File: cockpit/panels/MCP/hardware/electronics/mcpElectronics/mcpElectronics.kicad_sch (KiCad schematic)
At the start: 12 parts

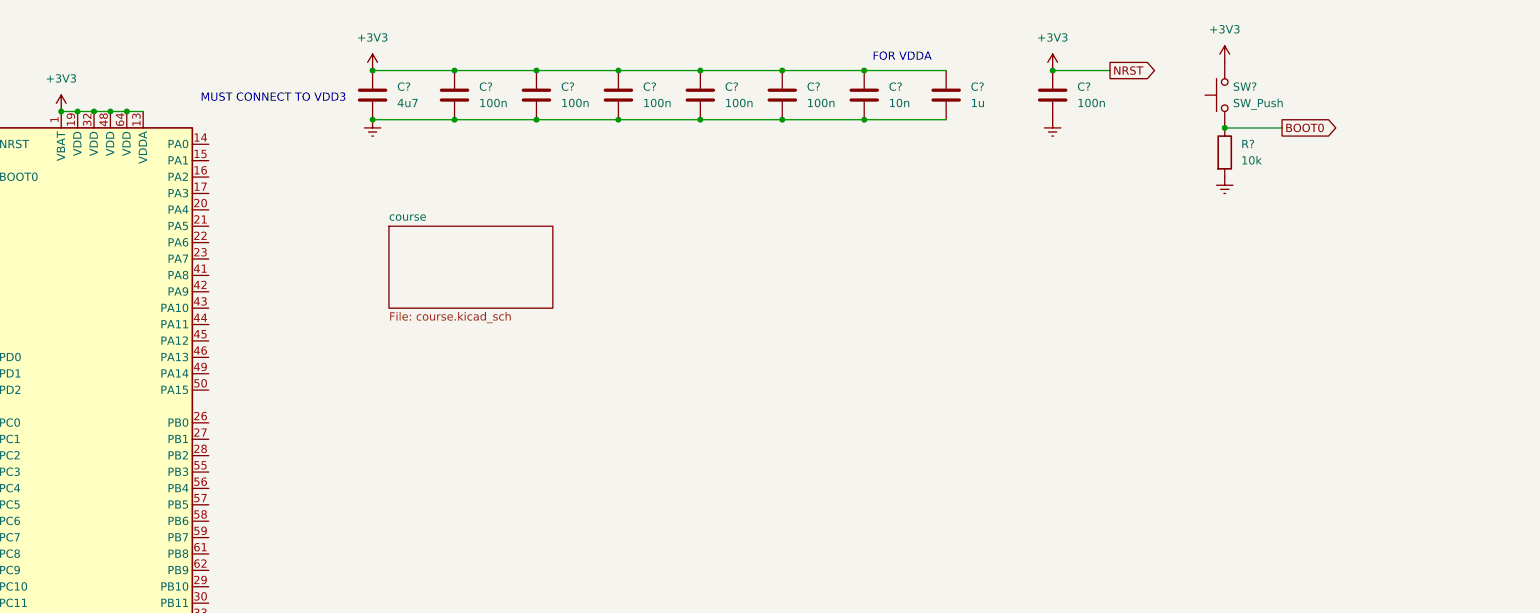
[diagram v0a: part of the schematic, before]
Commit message: add more course display circuitry
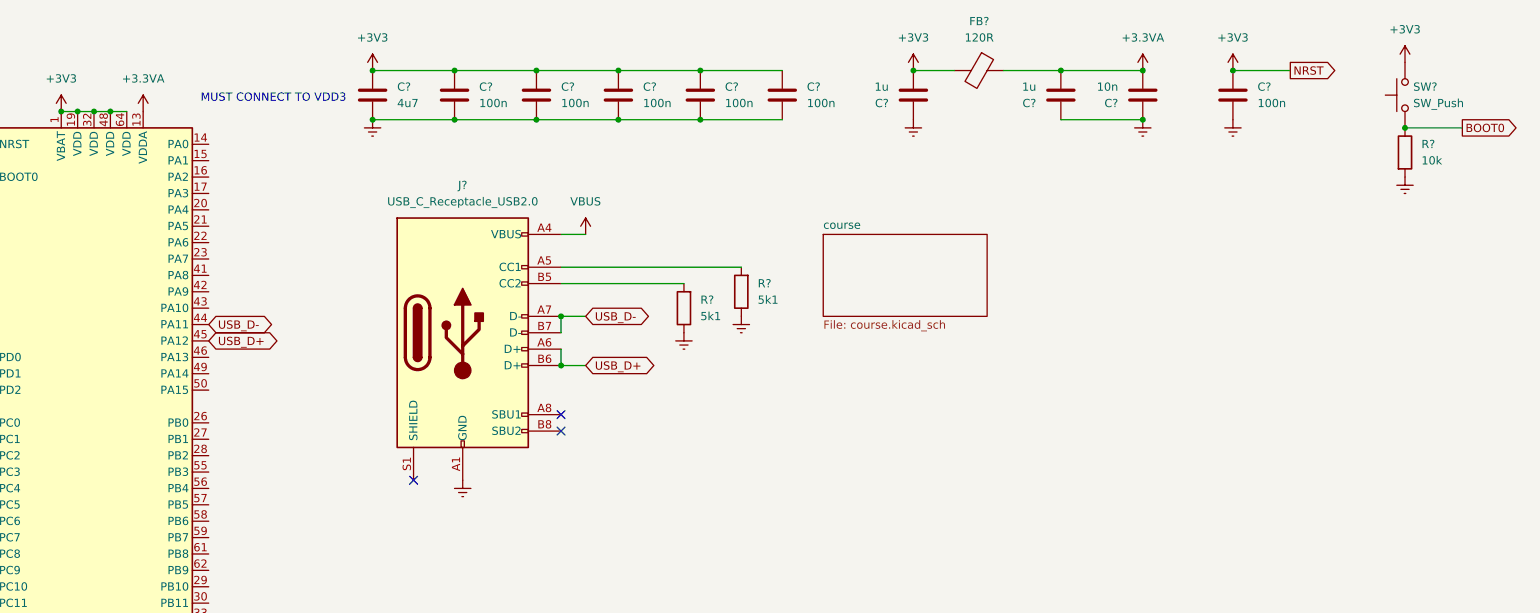
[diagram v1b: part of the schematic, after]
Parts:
- removed C?: 1u, symbol Device:C
- removed C?: 10n, symbol Device:C
- added C?: 10n, symbol Device:C
- added C? (x2): 1u, symbol Device:C
- added FB?: 120R, symbol Device:FerriteBead
- added J?: USB_C_Receptacle_USB2.0, symbol Connector:USB_C_Receptacle_USB2.0
- added R? (x2): 5k1, symbol Device:R
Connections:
- net +3V3: now also C?.2, FB?.2; no longer U?.13 (VDDA)
- net Earth: now also C?.1, C?.1, C?.1, J?.A1 (GND), J?.A12 (GND), J?.B1 (GND), J?.B12 (GND), R?.1, R?.1
- net USB_D-: now reaches U?.44 (PA11)
- net USB_D-: now also J?.A7 (D-), J?.B7 (D-)
- net USB_D+: now reaches U?.45 (PA12)
- net USB_D+: now also J?.A6 (D+), J?.B6 (D+)
- new net: J?.A5 (CC1), R?.2
- new net: J?.B5 (CC2), R?.2
- new net +3.3VA: C?.2, C?.2, FB?.1, U?.13 (VDDA)
- new net VBUS: J?.A4 (VBUS), J?.A9 (VBUS), J?.B4 (VBUS), J?.B9 (VBUS)
- no-connect marks 0 -> 3
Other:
- note removed: "FOR VDDA"
- moved on the sheet: C?, R?, SW?

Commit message: add electronics
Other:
- added sheet altitude (altitude.kicad_sch)
- added sheet ap (ap.kicad_sch)
- added sheet heading (heading.kicad_sch)
- added sheet iasmach (iasmach.kicad_sch)
- added sheet indication lights (indication_lights.kicad_sch)
- added sheet vert speed (vert_speed.kicad_sch)
- note added: "LED segments ordered LEAST SIGNIFICANT DIGIT FIRST"

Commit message: update schematic
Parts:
- removed C?: 100n, symbol Device:C
- removed U?: STM32F103R8T6TR, Package_QFP:LQFP-64_10x10mm_P0.5mm, symbol MCU_ST_STM32F1:STM32F103R8Tx
- added C?: 1u, symbol Device:C
- added C?: 10n, symbol Device:C
- added U?: STM32F302VBTx, Package_QFP:LQFP-100_14x14mm_P0.5mm, symbol MCU_ST_STM32F3:STM32F302VBTx
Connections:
- net +3.3VA: now also U?.22 (VDDA)
- net +3V3: now also C?.1, C?.1, U?.100 (VDD), U?.14 (NRST), U?.21 (VREF+), U?.28 (VDD), U?.50 (VDD), U?.6 (VBAT), U?.75 (VDD)
- net BOOT0: now also U?.94 (BOOT0)
- net Earth: now also U?.20 (VSSA), U?.49 (VSS), U?.74 (VSS), U?.99 (VSS)
- net USB_D+: now also U?.71 (PA12)
- net USB_D-: now also U?.70 (PA11)
- new net: C?.2, C?.2
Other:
- added sheet general (general.kicad_sch)
- note added: "NEED TO BE ABLE TO DIM DISPLAY LEDS"
- note added: "need to add backlight to buttons"
- note removed: "MUST CONNECT TO VDD3"
- moved on the sheet: C?, FB?, J?, R?, SW?

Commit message: update
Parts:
- removed U?: STM32F302VBTx, Package_QFP:LQFP-100_14x14mm_P0.5mm, symbol MCU_ST_STM32F3:STM32F302VBTx
- added C27, C28, C29, C30, C31, C32, C33, C34, C35: 100n, Capacitor_SMD:C_0402_1005Metric, symbol Device:C
- added C36, C37: 2u2, Capacitor_SMD:C_0402_1005Metric, symbol Device:C
- added U15: STM32F429ZETx, Package_QFP:LQFP-144_20x20mm_P0.5mm, symbol MCU_ST_STM32F4:STM32F429ZETx
- C38, C39, C40, C41, C42, C43, C44, C45, C46, C47, C48: renamed from C?; footprint (none) -> Capacitor_SMD:C_0402_1005Metric
- FB1: renamed from FB?; footprint (none) -> Inductor_SMD:L_0402_1005Metric
- J14: renamed from J?; footprint (none) -> Connector_USB:USB_C_Receptacle_HRO_TYPE-C-31-M-12
- R108, R109, R110: renamed from R?; footprint (none) -> Resistor_SMD:R_0402_1005Metric
- SW1: renamed from SW?; footprint (none) -> Button_Switch_THT:SW_PUSH_6mm_H5mm
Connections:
- net +3.3VA: now also U15.33 (VDDA)
- net +3V3: now also C27.1, C28.1, C29.1, C30.1, C31.1, C32.1, C33.1, C34.1, C35.1, U15.108 (VDD), U15.121 (VDD), U15.131 (VDD), U15.144 (VDD), U15.17 (VDD), U15.30 (VDD), U15.32 (VREF+), U15.39 (VDD), U15.52 (VDD), U15.6 (VBAT), U15.62 (VDD), U15.72 (VDD), U15.84 (VDD), U15.95 (VDD); no longer C48.1
- net ALTITUDE_DEC: now also U15.56 (PG0)
- net ALTITUDE_INC: now also U15.57 (PG1)
- net ALT_HLD_PUSH: now also U15.136 (PB6)
- net ALT_INTV_PUSH: now also U15.60 (PE9)
- net APP_PUSH: now also U15.126 (PG11)
- net A/P_DISENGAGE: now also U15.89 (PG4)
- net A/T_ARM_ON: now also U15.100 (PA8)
- net BANK_ANGLE_SELECT: now also U15.139 (PB8)
- net BOOT0: now also U15.138 (BOOT0)
- net CMD_A_PUSH: now also U15.70 (PB11)
- net CMD_B_PUSH: now also U15.73 (PB12)
- net COURSE_CA_DEC: now also U15.77 (PD8)
- net COURSE_CA_INC: now also U15.78 (PD9)
- net COURSE_FO_DEC: now also U15.92 (PG7)
- net COURSE_FO_INC: now also U15.91 (PG6)
- net CWS_A_PUSH: now also U15.74 (PB13)
- net CWS_B_PUSH: now also U15.88 (PG3)
- net C/O_PUSH: now also U15.2 (PE3)
- net Earth: now also C40.2, C42.2, C27.2, C28.2, C29.2, C30.2, C31.2, C32.2, C33.2, C34.2, C35.2, C36.2, C37.2, U15.107 (VSS), U15.120 (VSS), U15.130 (VSS), U15.16 (VSS), U15.31 (VSSA), U15.38 (VSS), U15.51 (VSS), U15.61 (VSS), U15.83 (VSS), U15.94 (VSS)
- net F/D_A_ON: now also U15.41 (PA5)
- net F/D_B_ON: now also U15.90 (PG5)
- net HDG_SEL_PUSH: now also U15.118 (PD4)
- net HEADING_DEC: now also U15.141 (PE0)
- net HEADING_INC: now also U15.140 (PB9)
- net IASMACH_DEC: now also U15.45 (PC5)
- net IASMACH_INC: now also U15.46 (PB0)
- net LNAV_PUSH: now also U15.49 (PF11)
- net LVL_CHG_PUSH: now also U15.110 (PA15)
- net N1_PUSH: now also U15.112 (PC11)
- net SPD_INTV_PUSH: now also U15.42 (PA6)
- net SPEED_PUSH: now also U15.111 (PC10)
- net USB_D+: now also U15.104 (PA12)
- net USB_D-: now also U15.103 (PA11)
- net VBUS: now also U15.101 (PA9)
- net VERT_SPEED_DEC: now also U15.68 (PE15)
- net VERT_SPEED_INC: now also U15.69 (PB10)
- net VNAV_PUSH: now also U15.43 (PA7)
- net VOR_LOC_PUSH: now also U15.50 (PF12)
- new net: C37.1, U15.71 (VCAP_1)
- new net: C36.1, U15.106 (VCAP_2)
- new net ALT_HLD_IND: U15.125 (PG10)
- new net APP_IND: U15.124 (PG9)
- new net A/T_ARM_IND: U15.123 (PD7)
- new net A/T_TOGGLE_RESET: U15.102 (PA10)
- new net BACKLIGHT_CONTROL: U15.98 (PC8)
- new net CMD_A_IND: U15.128 (PG13)
- new net CMD_B_IND: U15.129 (PG14)
- new net CWS_A_IND: U15.132 (PG15)
- new net CWS_B_IND: U15.133 (PB3)
- new net HDG_SEL_IND: U15.115 (PD1)
- new net LED_MULTIPLEX_0: U15.3 (PE4)
- new net LED_MULTIPLEX_1: U15.4 (PE5)
- new net LED_MULTIPLEX_10: U15.47 (PB1)
- new net LED_MULTIPLEX_11: U15.44 (PC4)
- new net LED_MULTIPLEX_12: U15.59 (PE8)
- new net LED_MULTIPLEX_13: U15.58 (PE7)
- new net LED_MULTIPLEX_14: U15.55 (PF15)
- new net LED_MULTIPLEX_15: U15.54 (PF14)
- new net LED_MULTIPLEX_16: U15.53 (PF13)
- new net LED_MULTIPLEX_17: U15.64 (PE11)
- new net LED_MULTIPLEX_18: U15.65 (PE12)
- new net LED_MULTIPLEX_19: U15.66 (PE13)
- new net LED_MULTIPLEX_2: U15.5 (PE6)
- new net LED_MULTIPLEX_20: U15.67 (PE14)
- new net LED_MULTIPLEX_21: U15.63 (PE10)
- new net LED_MULTIPLEX_22: U15.1 (PE2)
- new net LED_MULTIPLEX_23: U15.142 (PE1)
- new net LED_MULTIPLEX_3: U15.79 (PD10)
- new net LED_MULTIPLEX_4: U15.80 (PD11)
- new net LED_MULTIPLEX_5: U15.87 (PG2)
- new net LED_MULTIPLEX_6: U15.97 (PC7)
- new net LED_MULTIPLEX_7: U15.96 (PC6)
- new net LED_MULTIPLEX_8: U15.93 (PG8)
- new net LED_MULTIPLEX_9: U15.48 (PB2)
- new net LED_MULTIPLEX_A: U15.75 (PB14)
- new net LED_MULTIPLEX_B: U15.76 (PB15)
- new net LED_MULTIPLEX_C: U15.81 (PD12)
- new net LED_MULTIPLEX_D: U15.82 (PD13)
- new net LED_MULTIPLEX_E: U15.85 (PD14)
- new net LED_MULTIPLEX_F: U15.86 (PD15)
- new net LED_MULTIPLEX_G: U15.99 (PC9)
- new net LNAV_IND: U15.114 (PD0)
- new net LVL_CHG_IND: U15.116 (PD2)
- new net MA_PRI_IND: U15.134 (PB4)
- new net MA_SEC_IND: U15.135 (PB5)
- new net N1_ARM_IND: U15.122 (PD6)
- new net NRST: C48.1, U15.25 (NRST)
- new net SPEED_ARM_IND: U15.119 (PD5)
- new net SWCLK: U15.109 (PA14)
- new net SWDIO: U15.105 (PA13)
- new net VNAV_IND: U15.117 (PD3)
- new net VOR_LOC_IND: U15.113 (PC12)
- new net V/S_IND: U15.127 (PG12)
- new net V/S_PUSH: U15.137 (PB7)
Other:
- added sheet power (power.kicad_sch)
- note added: "5V across leds in series with 500R for 10mA"
- note added: "PWM"
- note added: "VREF+"
- note removed: "LED segments ordered LEAST SIGNIFICANT DIGIT FIRST"
- note removed: "NEED TO BE ABLE TO DIM DISPLAY LEDS"
- note removed: "need to add backlight to buttons"
- moved on the sheet: C38, C39, C40, C41, C42, C43, C44, J14, R108, R109, R110, SW1
